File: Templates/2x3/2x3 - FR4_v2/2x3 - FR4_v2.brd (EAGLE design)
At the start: 83.2 x 57.8 mm, 1 part

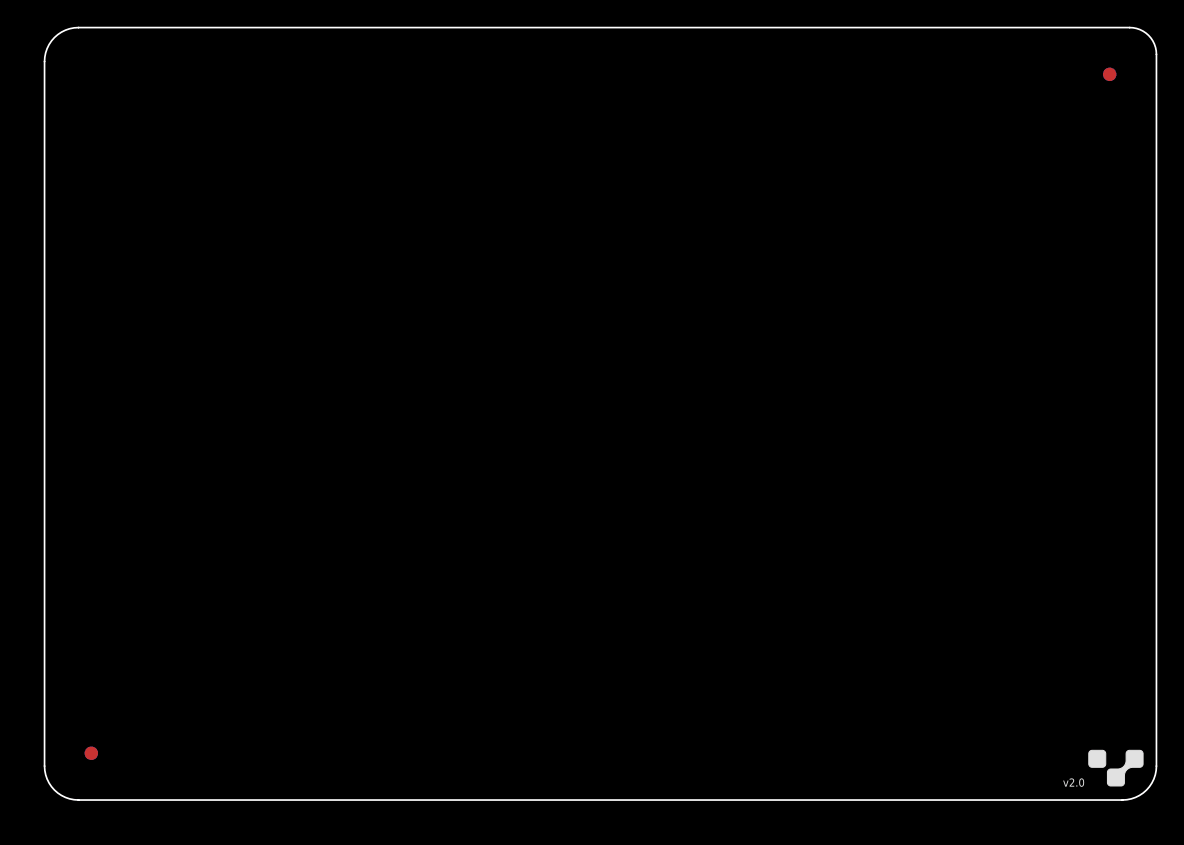
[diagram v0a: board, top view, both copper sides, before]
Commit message: Updated 4x5 to make fiducial a bit smaller to meet our bounds. Added 'fr4' silkscreen to 2x3, 3x4 and 4x5 substrates
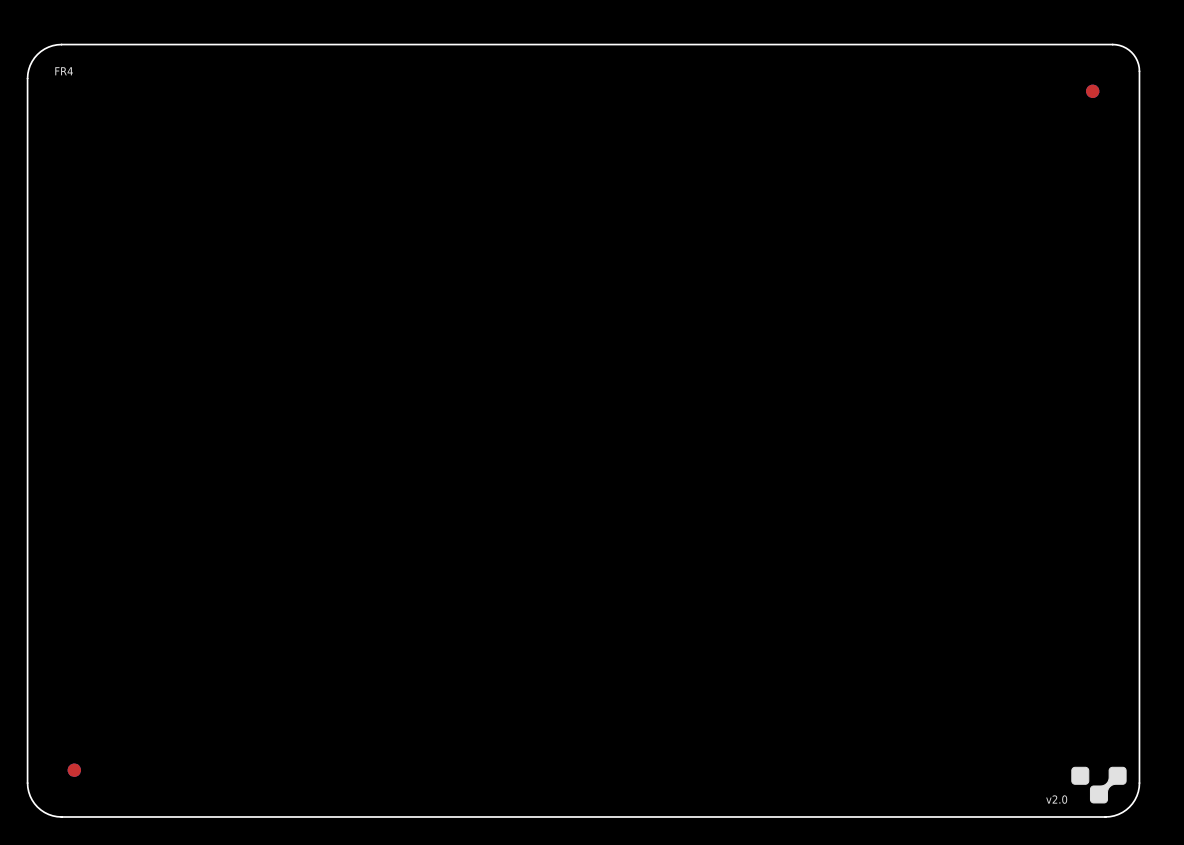
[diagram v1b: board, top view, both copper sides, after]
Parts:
- moved E$1 1.80 mm to (-1.27, -1.27)
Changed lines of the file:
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@@
 <?xml version="1.0" encoding="utf-8"?>
 <!DOCTYPE eagle SYSTEM "eagle.dtd">
-<eagle version="9.0.1">
+<eagle version="9.3.2">
 <drawing>
 <settings>
@@
 <param name="checkStop" value="0"/>
 <param name="checkValues" value="0"/>
+<param name="checkNames" value="1"/>
+<param name="checkWireStubs" value="1"/>
+<param name="checkPolygonWidth" value="0"/>
 <param name="useDiameter" value="13"/>
 <param name="maxErrors" value="50"/>
@@
 </autorouter>
 <elements>
-<element name="E$1" library="voltera_community_lib" package="2X3_BOARD_V2" value="" x="0" y="0"/>
+<element name="E$1" library="voltera_community_lib" package="2X3_BOARD_V2" value="" x="-1.27" y="-1.27" smashed="yes"/>
 </elements>
 <signals>
 </signals>
+<mfgpreviewcolors>
+<mfgpreviewcolor name="soldermaskcolor" color="0xC8008000"/>
+<mfgpreviewcolor name="silkscreencolor" color="0xFFFEFEFE"/>
+<mfgpreviewcolor name="backgroundcolor" color="0xFF282828"/>
+<mfgpreviewcolor name="coppercolor" color="0xFFFFBF00"/>
+<mfgpreviewcolor name="substratecolor" color="0xFF786E46"/>
+</mfgpreviewcolors>
 </board>
 </drawing>
